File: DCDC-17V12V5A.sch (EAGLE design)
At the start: 36 parts, among them CN2 2828XX-2282834-2, CN3 2828XX-2282834-2, Q10 NMOSFET, Q9 NMOSFET, U1 LM3150MHX/NOPB

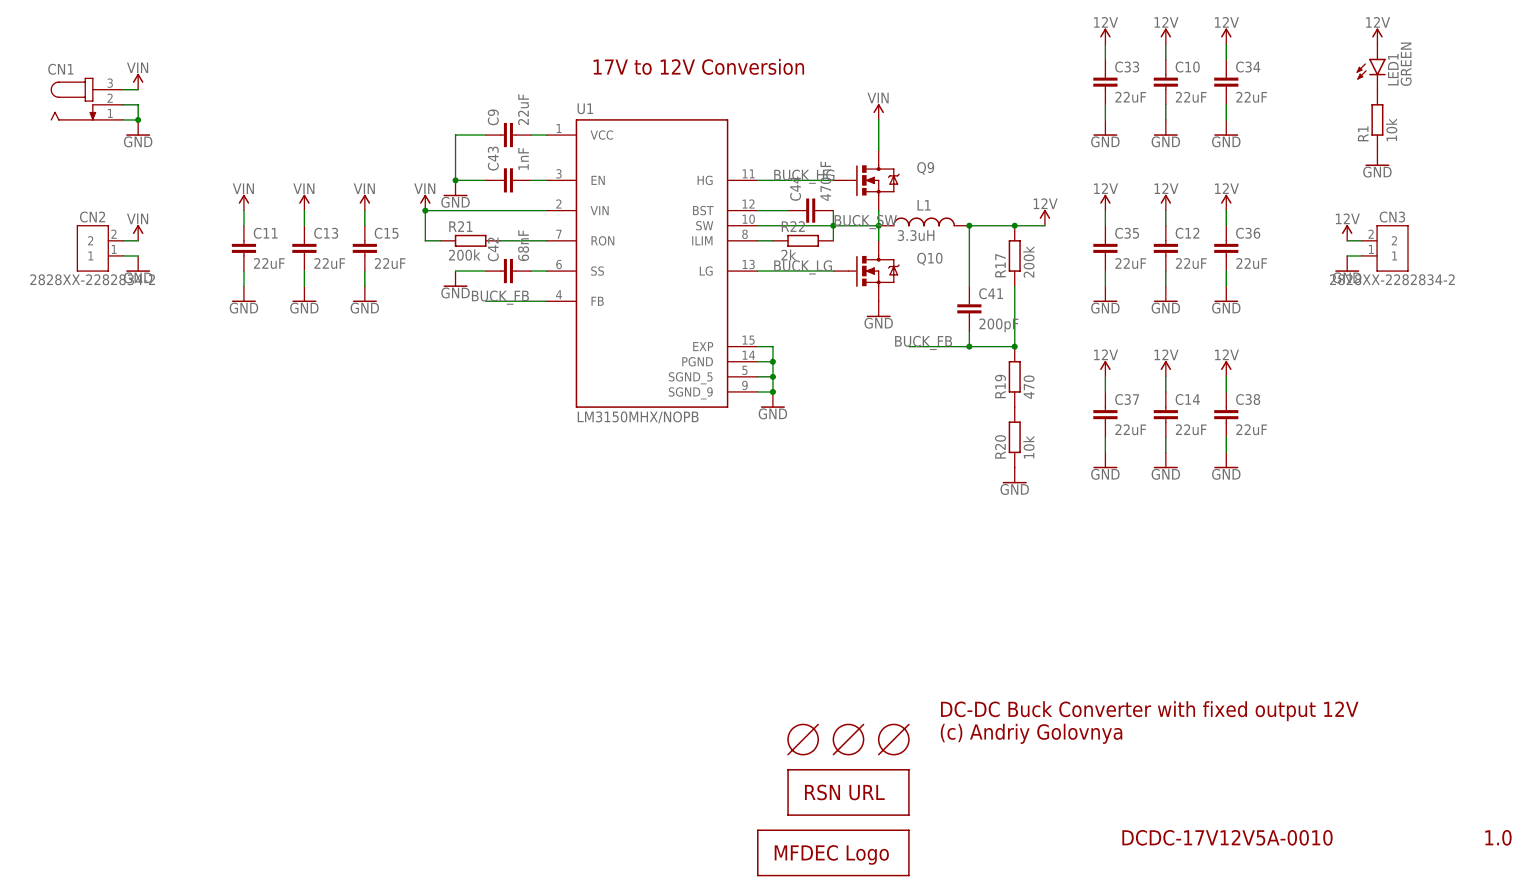
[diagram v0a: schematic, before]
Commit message: Improved layout of DC-DC board. Rotated input terminal. Generated CAM files. Generated BoM and PnP files. Generated PNG preview. Generated PDF schematics.
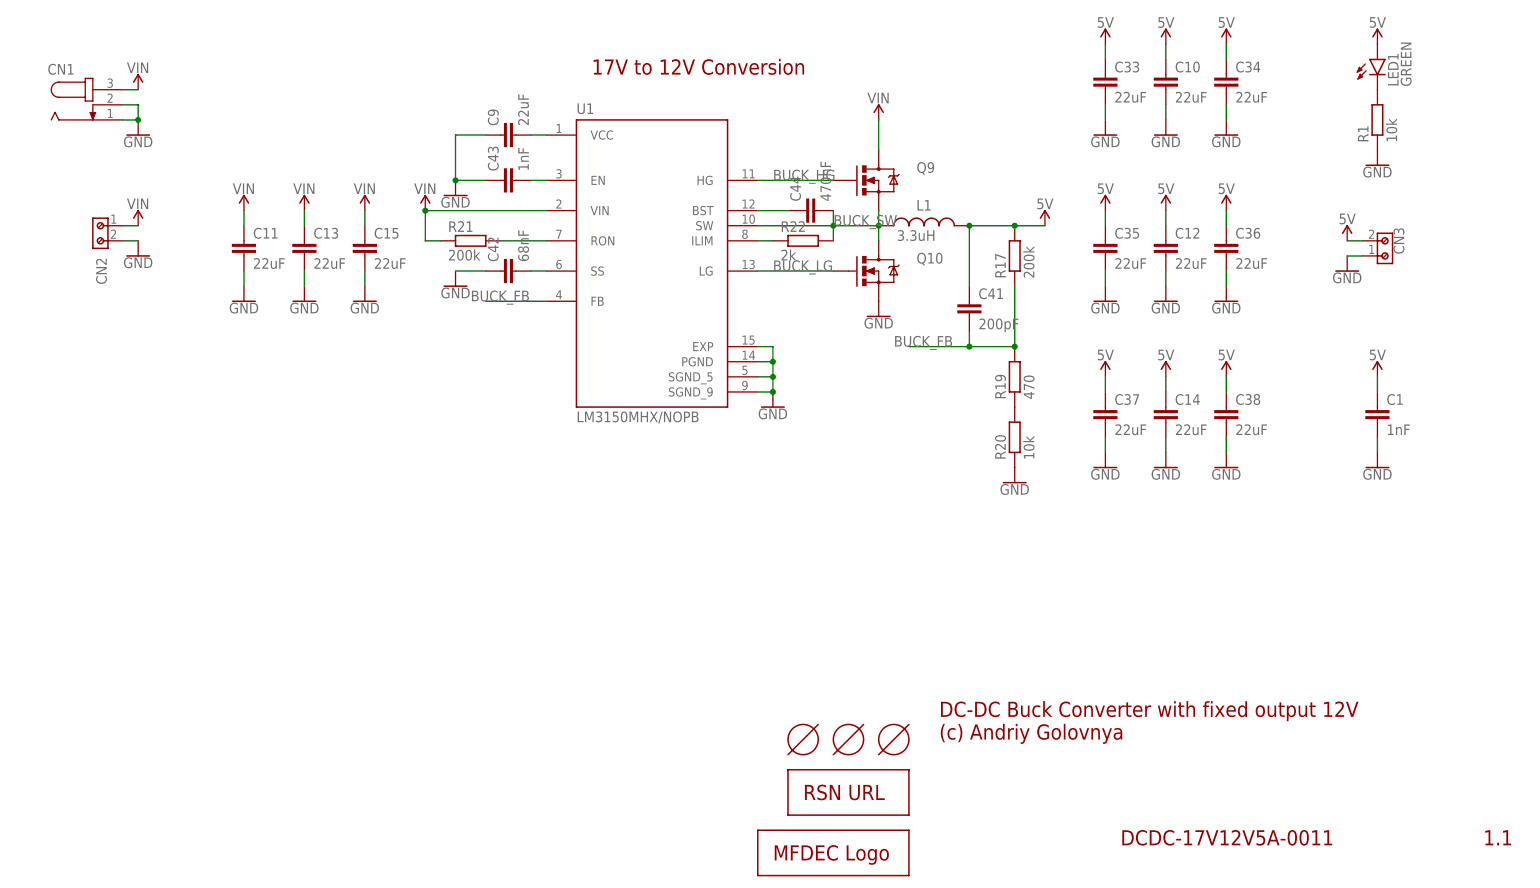
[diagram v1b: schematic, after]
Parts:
- added C1: 1nF, rcl:C-EUC0603K
- CN2, CN3: value 2828XX-2282834-2 -> (none); device Connector:2828XX-2282834-2 -> Wurth_Connectors_WR-TBL Rising Cage Clamp:691213510002
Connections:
- net N$16 renamed BUCK_SS
- net N$18 renamed BUCK_EN
- net N$19 renamed BUCK_VCC
- net N$21 renamed BUCK_RON
- net N$23 renamed BUCK_BST
- net N$8 renamed BUCK_ILIM
- removed net 12V: C10.1, C12.1, C14.1, C33.1, C34.1, C35.1, C36.1, C37.1, C38.1, C41.1, CN3.2, L1.2, LED1.A, R17.2
- new net 5V: C1.1, C10.1, C12.1, C14.1, C33.1, C34.1, C35.1, C36.1, C37.1, C38.1, C41.1, CN3.2, L1.2, LED1.A, R17.2
- net GND: now also C1.2, CN2.2; no longer CN2.1
- net VIN: now also CN2.1; no longer CN2.2
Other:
- note added: "1.1"
- note added: "DCDC-17V12V5A-0011"
- note removed: "1.0"
- note removed: "DCDC-17V12V5A-0010"

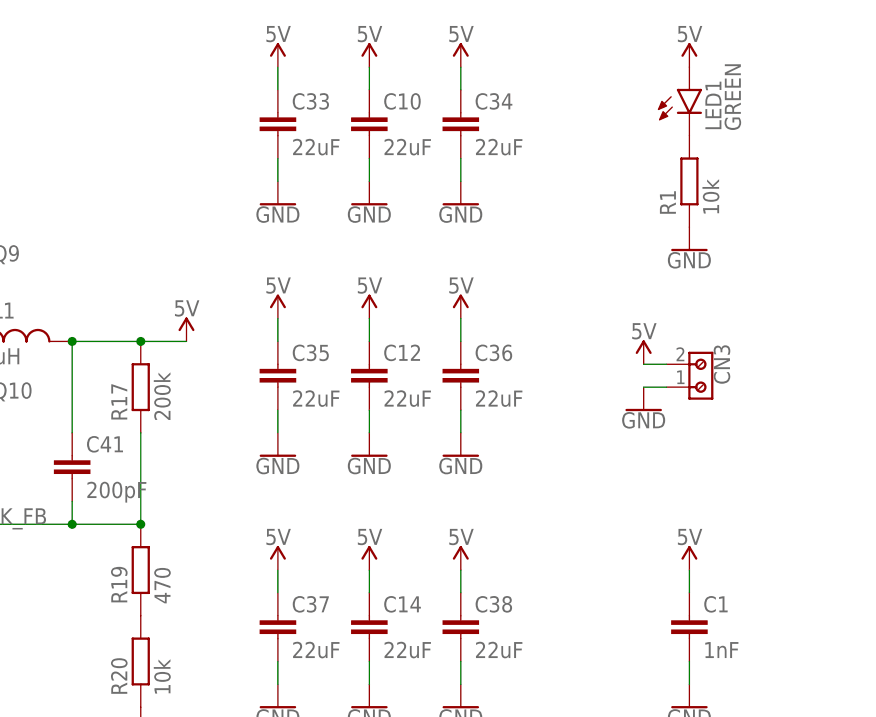
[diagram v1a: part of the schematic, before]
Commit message: Added proper voltage symbols on 3.3v and 12v boards. Generated PDF schematics.
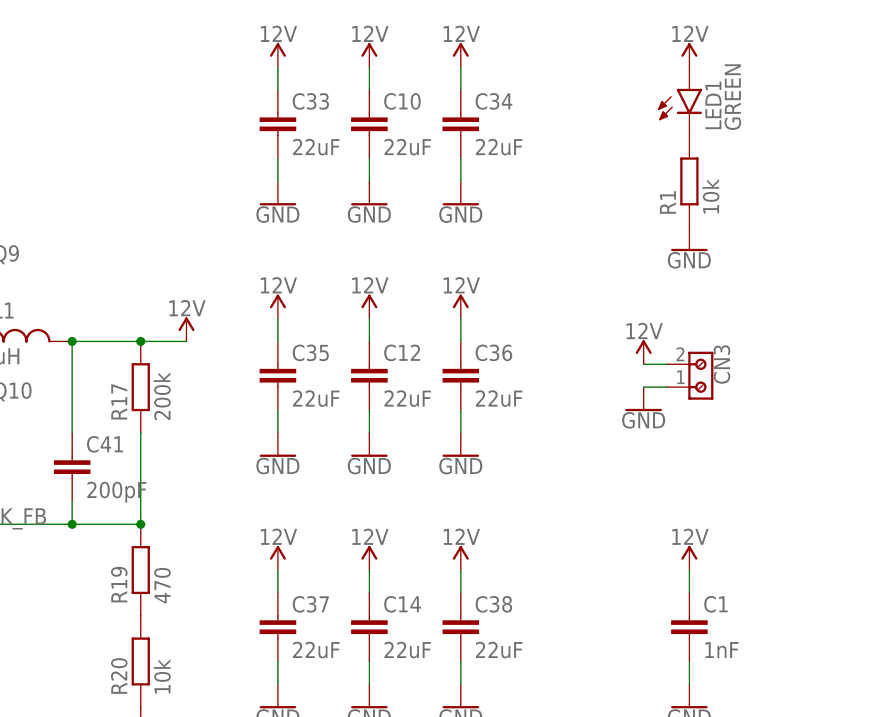
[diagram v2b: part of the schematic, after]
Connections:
- net 5V renamed 12V
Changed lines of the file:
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@@
 <part name="C37" library="rcl" library_urn="urn:adsk.eagle:library:334" deviceset="C-EU" device="C0805K" package3d_urn="urn:adsk.eagle:package:23681/2" value="22uF"/>
 <part name="C38" library="rcl" library_urn="urn:adsk.eagle:library:334" deviceset="C-EU" device="C0805K" package3d_urn="urn:adsk.eagle:package:23681/2" value="22uF"/>
-<part name="SUPPLY41" library="SparkFun-PowerSymbols" library_urn="urn:adsk.eagle:library:530" deviceset="5V" device=""/>
-<part name="SUPPLY42" library="SparkFun-PowerSymbols" library_urn="urn:adsk.eagle:library:530" deviceset="5V" device=""/>
-<part name="SUPPLY43" library="SparkFun-PowerSymbols" library_urn="urn:adsk.eagle:library:530" deviceset="5V" device=""/>
+<part name="SUPPLY41" library="SparkFun-PowerSymbols" library_urn="urn:adsk.eagle:library:530" deviceset="12V" device=""/>
+<part name="SUPPLY42" library="SparkFun-PowerSymbols" library_urn="urn:adsk.eagle:library:530" deviceset="12V" device=""/>
+<part name="SUPPLY43" library="SparkFun-PowerSymbols" library_urn="urn:adsk.eagle:library:530" deviceset="12V" device=""/>
 <part name="U1" library="LM3150MHX_NOPB" deviceset="LM3150MHX/NOPB" device=""/>
 <part name="Q9" library="BeagleBone_Blue_R3" library_urn="urn:adsk.eagle:library:5828899" deviceset="MOSFET-NCHANNEL" device="FDD8780" package3d_urn="urn:adsk.eagle:package:5829549/1" value="NMOSFET"/>
@@
 <part name="GND51" library="SparkFun-PowerSymbols" library_urn="urn:adsk.eagle:library:530" deviceset="GND" device=""/>
 <part name="L1" library="Wurth_Automotive_WE-CHSA" library_urn="urn:adsk.eagle:library:14076700" deviceset="WE-CHSA_1011" device="" package3d_urn="urn:adsk.eagle:package:13154812/4" technology="_7843330330" value="3.3uH"/>
-<part name="SUPPLY45" library="SparkFun-PowerSymbols" library_urn="urn:adsk.eagle:library:530" deviceset="5V" device=""/>
+<part name="SUPPLY45" library="SparkFun-PowerSymbols" library_urn="urn:adsk.eagle:library:530" deviceset="12V" device=""/>
 <part name="GND52" library="SparkFun-PowerSymbols" library_urn="urn:adsk.eagle:library:530" deviceset="GND" device=""/>
 <part name="SUPPLY46" library="SparkFun-PowerSymbols" library_urn="urn:adsk.eagle:library:530" deviceset="VIN" device=""/>
@@
 <part name="SUPPLY3" library="SparkFun-PowerSymbols" library_urn="urn:adsk.eagle:library:530" deviceset="VIN" device=""/>
 <part name="SUPPLY5" library="SparkFun-PowerSymbols" library_urn="urn:adsk.eagle:library:530" deviceset="VIN" device=""/>
-<part name="SUPPLY8" library="SparkFun-PowerSymbols" library_urn="urn:adsk.eagle:library:530" deviceset="5V" device=""/>
-<part name="SUPPLY47" library="SparkFun-PowerSymbols" library_urn="urn:adsk.eagle:library:530" deviceset="5V" device=""/>
-<part name="SUPPLY48" library="SparkFun-PowerSymbols" library_urn="urn:adsk.eagle:library:530" deviceset="5V" device=""/>
-<part name="SUPPLY49" library="SparkFun-PowerSymbols" library_urn="urn:adsk.eagle:library:530" deviceset="5V" device=""/>
-<part name="SUPPLY50" library="SparkFun-PowerSymbols" library_urn="urn:adsk.eagle:library:530" deviceset="5V" device=""/>
-<part name="SUPPLY51" library="SparkFun-PowerSymbols" library_urn="urn:adsk.eagle:library:530" deviceset="5V" device=""/>
+<part name="SUPPLY8" library="SparkFun-PowerSymbols" library_urn="urn:adsk.eagle:library:530" deviceset="12V" device=""/>
+<part name="SUPPLY47" library="SparkFun-PowerSymbols" library_urn="urn:adsk.eagle:library:530" deviceset="12V" device=""/>
+<part name="SUPPLY48" library="SparkFun-PowerSymbols" library_urn="urn:adsk.eagle:library:530" deviceset="12V" device=""/>
+<part name="SUPPLY49" library="SparkFun-PowerSymbols" library_urn="urn:adsk.eagle:library:530" deviceset="12V" device=""/>
+<part name="SUPPLY50" library="SparkFun-PowerSymbols" library_urn="urn:adsk.eagle:library:530" deviceset="12V" device=""/>
+<part name="SUPPLY51" library="SparkFun-PowerSymbols" library_urn="urn:adsk.eagle:library:530" deviceset="12V" device=""/>
 <part name="GND58" library="SparkFun-PowerSymbols" library_urn="urn:adsk.eagle:library:530" deviceset="GND" device=""/>
 <part name="GND59" library="SparkFun-PowerSymbols" library_urn="urn:adsk.eagle:library:530" deviceset="GND" device=""/>
@@
 <part name="SUPPLY1" library="SparkFun-PowerSymbols" library_urn="urn:adsk.eagle:library:530" deviceset="VIN" device=""/>
 <part name="GND3" library="SparkFun-PowerSymbols" library_urn="urn:adsk.eagle:library:530" deviceset="GND" device=""/>
-<part name="SUPPLY6" library="SparkFun-PowerSymbols" library_urn="urn:adsk.eagle:library:530" deviceset="5V" device=""/>
+<part name="SUPPLY6" library="SparkFun-PowerSymbols" library_urn="urn:adsk.eagle:library:530" deviceset="12V" device=""/>
 <part name="LOGO1" library="_my_logos" deviceset="RSNURL" device="_QR_8MM" value="RSNURL_QR_8MM"/>
 <part name="LOGO2" library="_my_logos" deviceset="MFDECLOGO" device="_L_10MM" value="MFDECLOGO_L_10MM"/>
 <part name="LED1" library="led" library_urn="urn:adsk.eagle:library:259" deviceset="LED" device="SML0603" package3d_urn="urn:adsk.eagle:package:15832/1" value="GREEN"/>
 <part name="R1" library="rcl" library_urn="urn:adsk.eagle:library:334" deviceset="R-EU_" device="R0603" package3d_urn="urn:adsk.eagle:package:23555/3" value="10k"/>
-<part name="SUPPLY7" library="SparkFun-PowerSymbols" library_urn="urn:adsk.eagle:library:530" deviceset="5V" device=""/>
+<part name="SUPPLY7" library="SparkFun-PowerSymbols" library_urn="urn:adsk.eagle:library:530" deviceset="12V" device=""/>
 <part name="GND4" library="SparkFun-PowerSymbols" library_urn="urn:adsk.eagle:library:530" deviceset="GND" device=""/>
 <part name="HOLE1" library="_my_fiducia" deviceset="TOOLINGHOLE" device=""/>
@@
 <part name="HOLE3" library="_my_fiducia" deviceset="TOOLINGHOLE" device=""/>
 <part name="C1" library="rcl" library_urn="urn:adsk.eagle:library:334" deviceset="C-EU" device="C0603K" package3d_urn="urn:adsk.eagle:package:23680/2" value="1nF"/>
-<part name="SUPPLY9" library="SparkFun-PowerSymbols" library_urn="urn:adsk.eagle:library:530" deviceset="5V" device=""/>
+<part name="SUPPLY9" library="SparkFun-PowerSymbols" library_urn="urn:adsk.eagle:library:530" deviceset="12V" device=""/>
 <part name="GND5" library="SparkFun-PowerSymbols" library_urn="urn:adsk.eagle:library:530" deviceset="GND" device=""/>
 <part name="SUPPLY4" library="SparkFun-PowerSymbols" library_urn="urn:adsk.eagle:library:530" deviceset="VIN" device=""/>
@@
 </segment>
 </net>
-<net name="5V" class="0">
+<net name="12V" class="0">
 <segment>
 <pinref part="C34" gate="G$1" pin="1"/>
 <wire x1="213.36" y1="139.7" x2="213.36" y2="142.24" width="0.1524" layer="91"/>
-<pinref part="SUPPLY43" gate="G$1" pin="5V"/>
+<pinref part="SUPPLY43" gate="G$1" pin="12V"/>
 </segment>
 <segment>
 <pinref part="C36" gate="G$1" pin="1"/>
 <wire x1="213.36" y1="111.76" x2="213.36" y2="114.3" width="0.1524" layer="91"/>
-<pinref part="SUPPLY42" gate="G$1" pin="5V"/>
+<pinref part="SUPPLY42" gate="G$1" pin="12V"/>
 </segment>
 <segment>
 <pinref part="C38" gate="G$1" pin="1"/>
 <wire x1="213.36" y1="83.82" x2="213.36" y2="86.36" width="0.1524" layer="91"/>
-<pinref part="SUPPLY41" gate="G$1" pin="5V"/>
+<pinref part="SUPPLY41" gate="G$1" pin="12V"/>
 </segment>
 <segment>
 <pinref part="L1" gate="G$1" pin="2"/>
-<pinref part="SUPPLY45" gate="G$1" pin="5V"/>
+<pinref part="SUPPLY45" gate="G$1" pin="12V"/>
 <pinref part="R17" gate="G$1" pin="2"/>
 <wire x1="170.18" y1="111.76" x2="177.8" y2="111.76" width="0.1524" layer="91"/>
@@
 <pinref part="C10" gate="G$1" pin="1"/>
 <wire x1="203.2" y1="142.24" x2="203.2" y2="139.7" width="0.1524" layer="91"/>
-<pinref part="SUPPLY8" gate="G$1" pin="5V"/>
+<pinref part="SUPPLY8" gate="G$1" pin="12V"/>
 </segment>
 <segment>
 <pinref part="C33" gate="G$1" pin="1"/>
 <wire x1="193.04" y1="142.24" x2="193.04" y2="139.7" width="0.1524" layer="91"/>
-<pinref part="SUPPLY47" gate="G$1" pin="5V"/>
+<pinref part="SUPPLY47" gate="G$1" pin="12V"/>
 </segment>
 <segment>
 <pinref part="C12" gate="G$1" pin="1"/>
 <wire x1="203.2" y1="114.3" x2="203.2" y2="111.76" width="0.1524" layer="91"/>
-<pinref part="SUPPLY48" gate="G$1" pin="5V"/>
+<pinref part="SUPPLY48" gate="G$1" pin="12V"/>
 </segment>
 <segment>
 <pinref part="C35" gate="G$1" pin="1"/>
 <wire x1="193.04" y1="114.3" x2="193.04" y2="111.76" width="0.1524" layer="91"/>
-<pinref part="SUPPLY49" gate="G$1" pin="5V"/>
+<pinref part="SUPPLY49" gate="G$1" pin="12V"/>
 </segment>
 <segment>
 <pinref part="C14" gate="G$1" pin="1"/>
 <wire x1="203.2" y1="86.36" x2="203.2" y2="83.82" width="0.1524" layer="91"/>
-<pinref part="SUPPLY50" gate="G$1" pin="5V"/>
+<pinref part="SUPPLY50" gate="G$1" pin="12V"/>
 </segment>
 <segment>
 <pinref part="C37" gate="G$1" pin="1"/>
 <wire x1="193.04" y1="86.36" x2="193.04" y2="83.82" width="0.1524" layer="91"/>
-<pinref part="SUPPLY51" gate="G$1" pin="5V"/>
-</segment>
-<segment>
-<pinref part="SUPPLY6" gate="G$1" pin="5V"/>
+<pinref part="SUPPLY51" gate="G$1" pin="12V"/>
+</segment>
+<segment>
+<pinref part="SUPPLY6" gate="G$1" pin="12V"/>
 <pinref part="CN3" gate="G$1" pin="2"/>
 <wire x1="233.68" y1="109.22" x2="236.22" y2="109.22" width="0.1524" layer="91"/>
@@
 <segment>
 <pinref part="LED1" gate="G$1" pin="A"/>
-<pinref part="SUPPLY7" gate="G$1" pin="5V"/>
+<pinref part="SUPPLY7" gate="G$1" pin="12V"/>
 </segment>
 <segment>
 <pinref part="C1" gate="G$1" pin="1"/>
-<pinref part="SUPPLY9" gate="G$1" pin="5V"/>
+<pinref part="SUPPLY9" gate="G$1" pin="12V"/>
 <wire x1="238.76" y1="83.82" x2="238.76" y2="86.36" width="0.1524" layer="91"/>
 </segment>

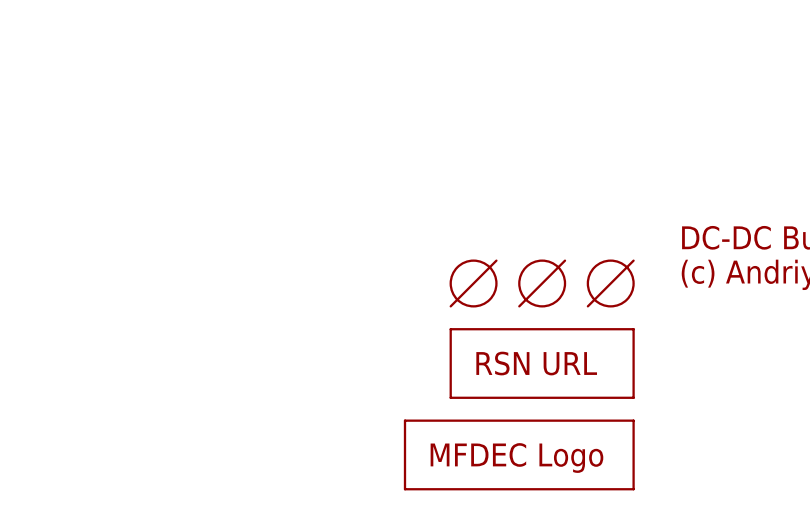
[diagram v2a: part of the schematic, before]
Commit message: Moved some texts and tooling holes a bit. Generated CAM files. Generated PNG preview. Generated PDF schematics. Renamed BoM and PnP files.
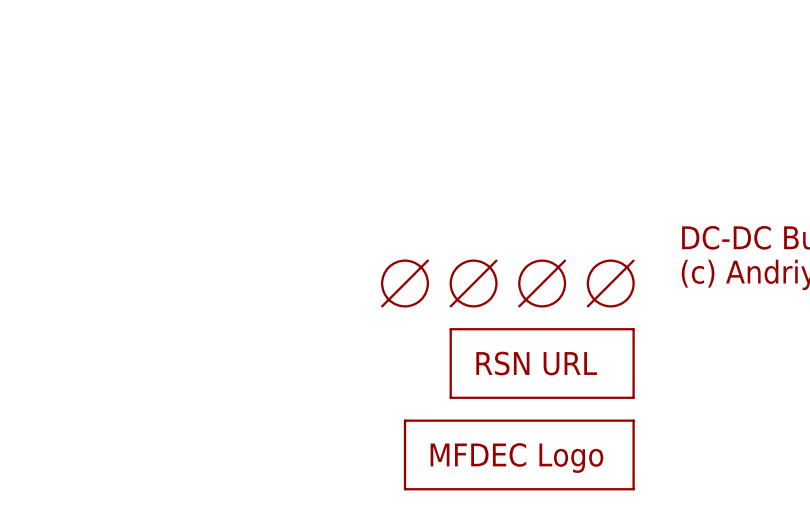
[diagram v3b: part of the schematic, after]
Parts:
- added HOLE4: TOOLINGHOLE, _my_fiducia:TOOLINGHOLE
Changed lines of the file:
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@@
 <part name="SUPPLY4" library="SparkFun-PowerSymbols" library_urn="urn:adsk.eagle:library:530" deviceset="VIN" device=""/>
 <part name="GND1" library="SparkFun-PowerSymbols" library_urn="urn:adsk.eagle:library:530" deviceset="GND" device=""/>
+<part name="HOLE4" library="_my_fiducia" deviceset="TOOLINGHOLE" device=""/>
 </parts>
 <sheets>
@@
 <attribute name="VALUE" x="30.48" y="106.426" size="1.778" layer="96" align="top-center"/>
 </instance>
+<instance part="HOLE4" gate="G$1" x="134.62" y="25.4" smashed="yes"/>
 </instances>
 <busses>
